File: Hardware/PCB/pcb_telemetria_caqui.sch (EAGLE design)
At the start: 42 parts

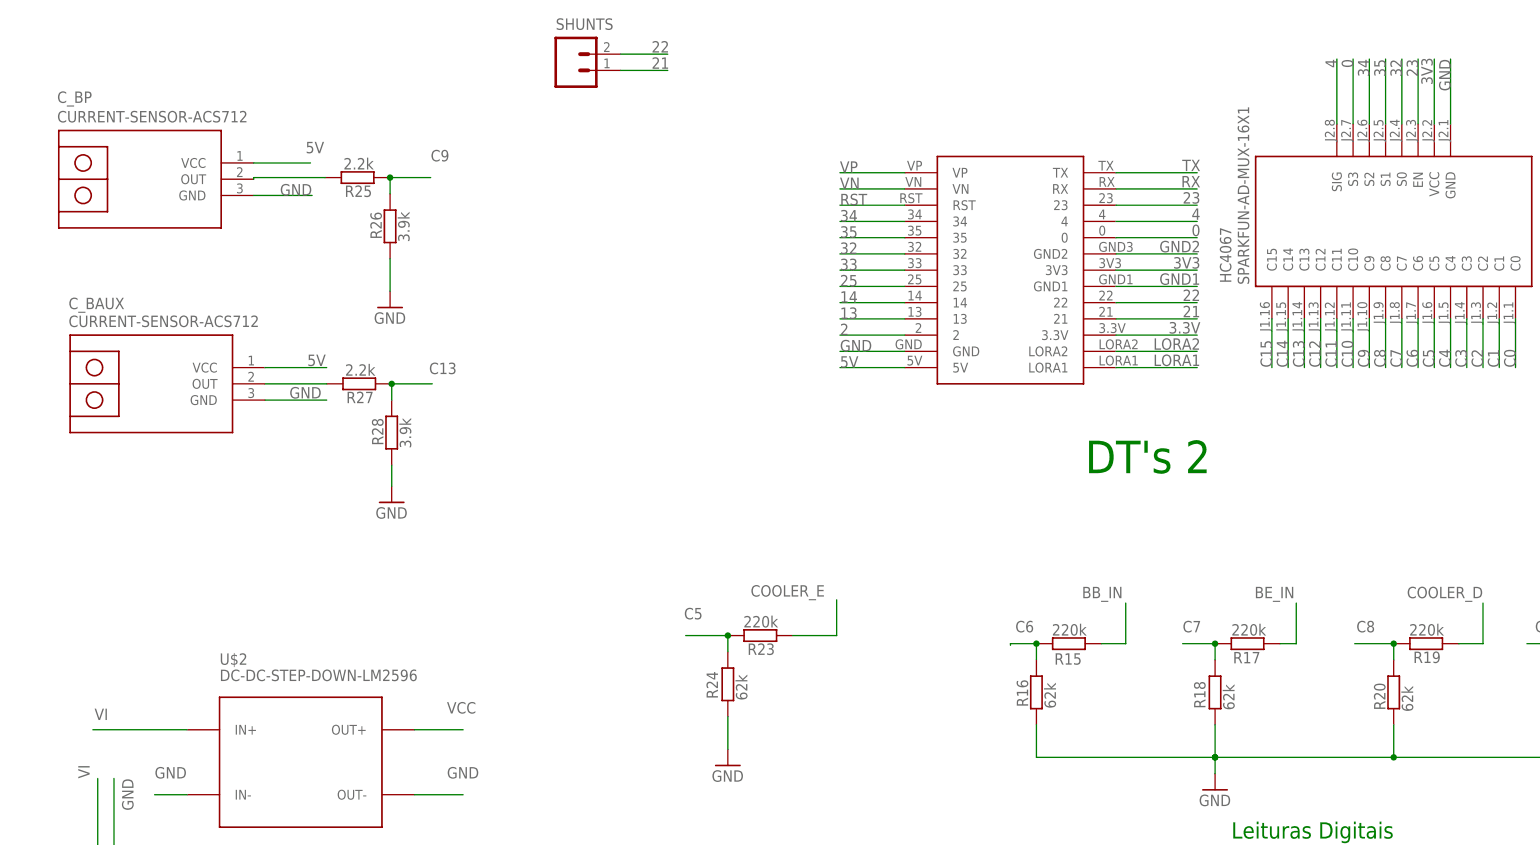
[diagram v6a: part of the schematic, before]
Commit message: Placa finalizada, aguardando ajustes
Finalizou-se o roteamento pre testes. Aguardando testes para realização de ajustes.
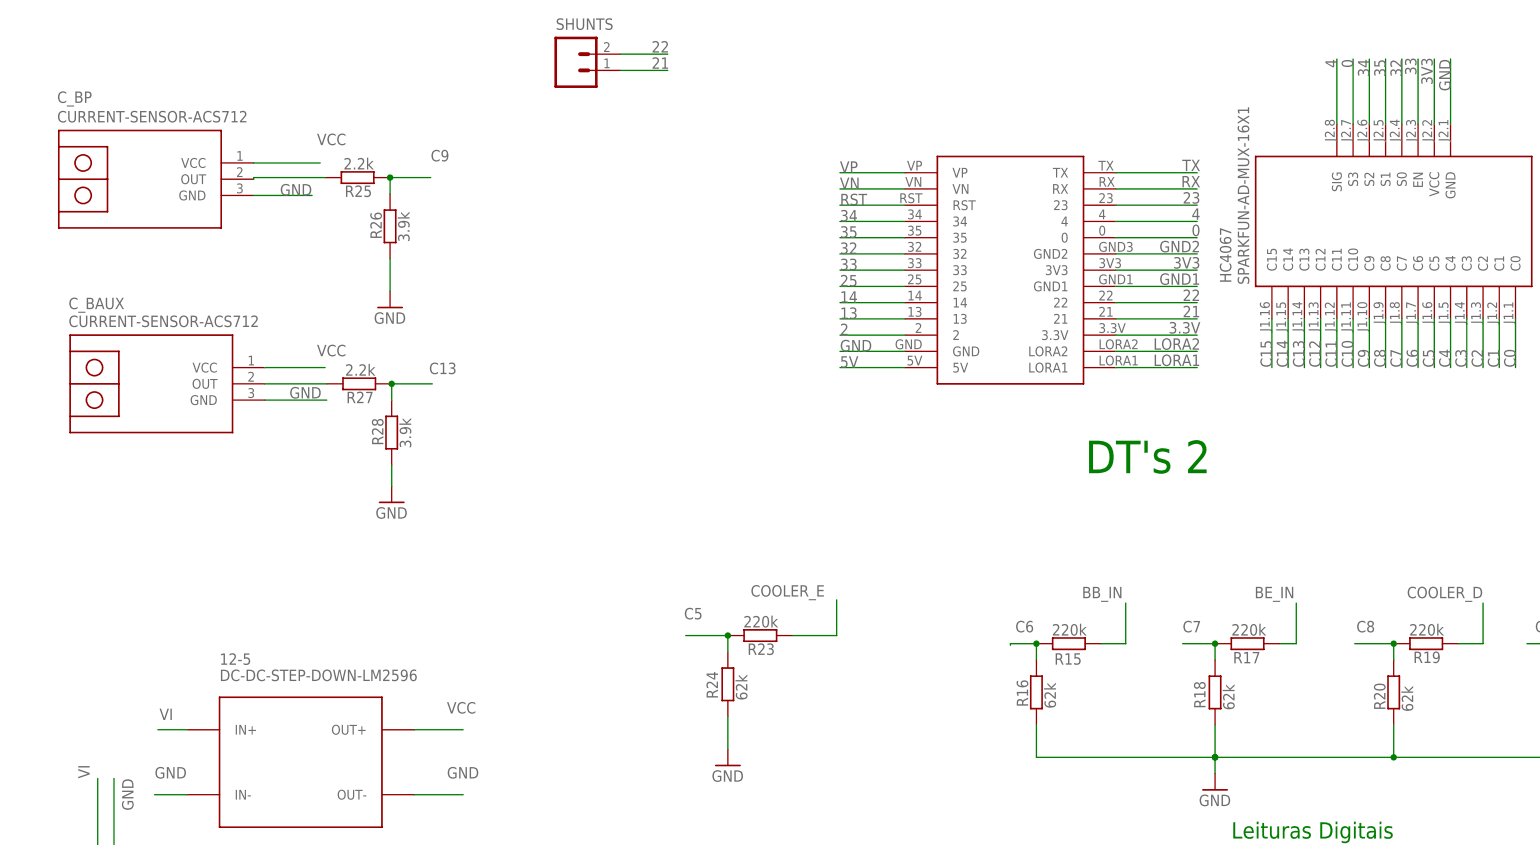
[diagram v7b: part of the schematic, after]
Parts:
- renumbered U$2 to 12-5
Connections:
- net 23: no longer HC4067.EN
- net 33: now also HC4067.EN
- net 5V: no longer C_BAUX.VCC, C_BP.VCC
- net VCC: now also C_BAUX.VCC, C_BP.VCC
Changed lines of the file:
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@@
 <?xml version="1.0" encoding="utf-8"?>
 <!DOCTYPE eagle SYSTEM "eagle.dtd">
-<eagle version="9.5.0">
+<eagle version="9.4.2">
 <drawing>
 <settings>
@@
 <part name="SUPPLY" library="con-amp-quick" library_urn="urn:adsk.eagle:library:125" deviceset="M02" device="" package3d_urn="urn:adsk.eagle:package:5956/1"/>
 <part name="TEMP2" library="con-amp-quick" library_urn="urn:adsk.eagle:library:125" deviceset="M02" device="" package3d_urn="urn:adsk.eagle:package:5956/1"/>
-<part name="U$2" library="diy-modules" deviceset="DC-DC-STEP-DOWN-LM2596" device=""/>
+<part name="12-5" library="diy-modules" deviceset="DC-DC-STEP-DOWN-LM2596" device=""/>
 </parts>
 <sheets>
@@
 <attribute name="NAME" x="-59.182" y="-58.928" size="1.778" layer="95"/>
 </instance>
-<instance part="U$2" gate="G$1" x="-134.62" y="50.8" smashed="yes">
+<instance part="12-5" gate="G$1" x="-134.62" y="50.8" smashed="yes">
 <attribute name="NAME" x="-147.32" y="66.04" size="1.778" layer="95"/>
 <attribute name="VALUE" x="-147.32" y="63.5" size="1.778" layer="96"/>
@@
 <wire x1="-40.132" y1="127.762" x2="-50.292" y2="127.762" width="0.1524" layer="91"/>
 <label x="-50.292" y="127.762" size="1.778" layer="95"/>
+</segment>
+<segment>
+<pinref part="HC4067" gate="G$1" pin="EN"/>
+<wire x1="40.132" y1="150.622" x2="40.132" y2="160.782" width="0.1524" layer="91"/>
+<label x="39.878" y="158.242" size="1.778" layer="95" rot="R90"/>
 </segment>
 </net>
@@
 </segment>
 <segment>
-<pinref part="U$2" gate="G$1" pin="IN-"/>
+<pinref part="12-5" gate="G$1" pin="IN-"/>
 <wire x1="-152.4" y1="45.72" x2="-157.48" y2="45.72" width="0.1524" layer="91"/>
 <label x="-157.48" y="48.26" size="1.778" layer="95"/>
 </segment>
 <segment>
-<pinref part="U$2" gate="G$1" pin="OUT-"/>
+<pinref part="12-5" gate="G$1" pin="OUT-"/>
 <wire x1="-116.84" y1="45.72" x2="-109.22" y2="45.72" width="0.1524" layer="91"/>
 <label x="-111.76" y="48.26" size="1.778" layer="95"/>
@@
 <label x="-50.292" y="112.522" size="1.778" layer="95"/>
 </segment>
-<segment>
-<pinref part="C_BAUX" gate="G$1" pin="VCC"/>
-<wire x1="-140.208" y1="112.522" x2="-130.556" y2="112.522" width="0.1524" layer="91"/>
-<label x="-133.604" y="112.776" size="1.778" layer="95"/>
-</segment>
-<segment>
-<pinref part="C_BP" gate="G$1" pin="VCC"/>
-<wire x1="-141.986" y1="144.526" x2="-133.096" y2="144.526" width="0.1524" layer="91"/>
-<label x="-133.858" y="146.05" size="1.778" layer="95"/>
-</segment>
 </net>
 <net name="TX" class="0">
@@
 <wire x1="-7.112" y1="137.922" x2="5.588" y2="137.922" width="0.1524" layer="91"/>
 <label x="6.096" y="138.176" size="1.778" layer="95" align="bottom-right"/>
-</segment>
-<segment>
-<pinref part="HC4067" gate="G$1" pin="EN"/>
-<wire x1="40.132" y1="150.622" x2="40.132" y2="160.782" width="0.1524" layer="91"/>
-<label x="40.132" y="160.782" size="1.778" layer="95" rot="R90" align="bottom-right"/>
 </segment>
 </net>
@@
 </segment>
 <segment>
-<pinref part="U$2" gate="G$1" pin="IN+"/>
-<wire x1="-152.4" y1="55.88" x2="-167.132" y2="55.88" width="0.1524" layer="91"/>
-<label x="-166.878" y="57.404" size="1.778" layer="95"/>
+<pinref part="12-5" gate="G$1" pin="IN+"/>
+<wire x1="-152.4" y1="55.88" x2="-156.972" y2="55.88" width="0.1524" layer="91"/>
+<label x="-156.718" y="57.404" size="1.778" layer="95"/>
 </segment>
 </net>
 <net name="VCC" class="0">
 <segment>
-<pinref part="U$2" gate="G$1" pin="OUT+"/>
+<pinref part="12-5" gate="G$1" pin="OUT+"/>
 <wire x1="-116.84" y1="55.88" x2="-109.22" y2="55.88" width="0.1524" layer="91"/>
 <label x="-111.76" y="58.42" size="1.778" layer="95"/>
 </segment>
-</net>
+<segment>
+<pinref part="C_BAUX" gate="G$1" pin="VCC"/>
+<wire x1="-140.208" y1="112.522" x2="-130.81" y2="112.522" width="0.1524" layer="91"/>
+<label x="-132.08" y="114.3" size="1.778" layer="95"/>
+</segment>
+<segment>
+<pinref part="C_BP" gate="G$1" pin="VCC"/>
+<wire x1="-141.986" y1="144.526" x2="-131.572" y2="144.526" width="0.1524" layer="91"/>
+<label x="-132.08" y="147.32" size="1.778" layer="95"/>
+</segment>
+</net>
